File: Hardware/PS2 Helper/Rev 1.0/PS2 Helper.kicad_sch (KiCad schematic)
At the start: 6 parts, among them J1 PORT, J2 Keyboard, U1 74HC595, U2 ATtiny85

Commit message: Housekeeping
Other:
- title: 6502 Keyboard Helper -> 6502 PS2 Helper
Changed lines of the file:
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@@
 	(paper "USLetter")
 	(title_block
-		(title "6502 Keyboard Helper")
-		(date "2025-09-23")
+		(title "6502 PS2 Helper")
+		(date "2025-09-24")
 		(rev "1.0")
 		(company "A.C. Wright Design")

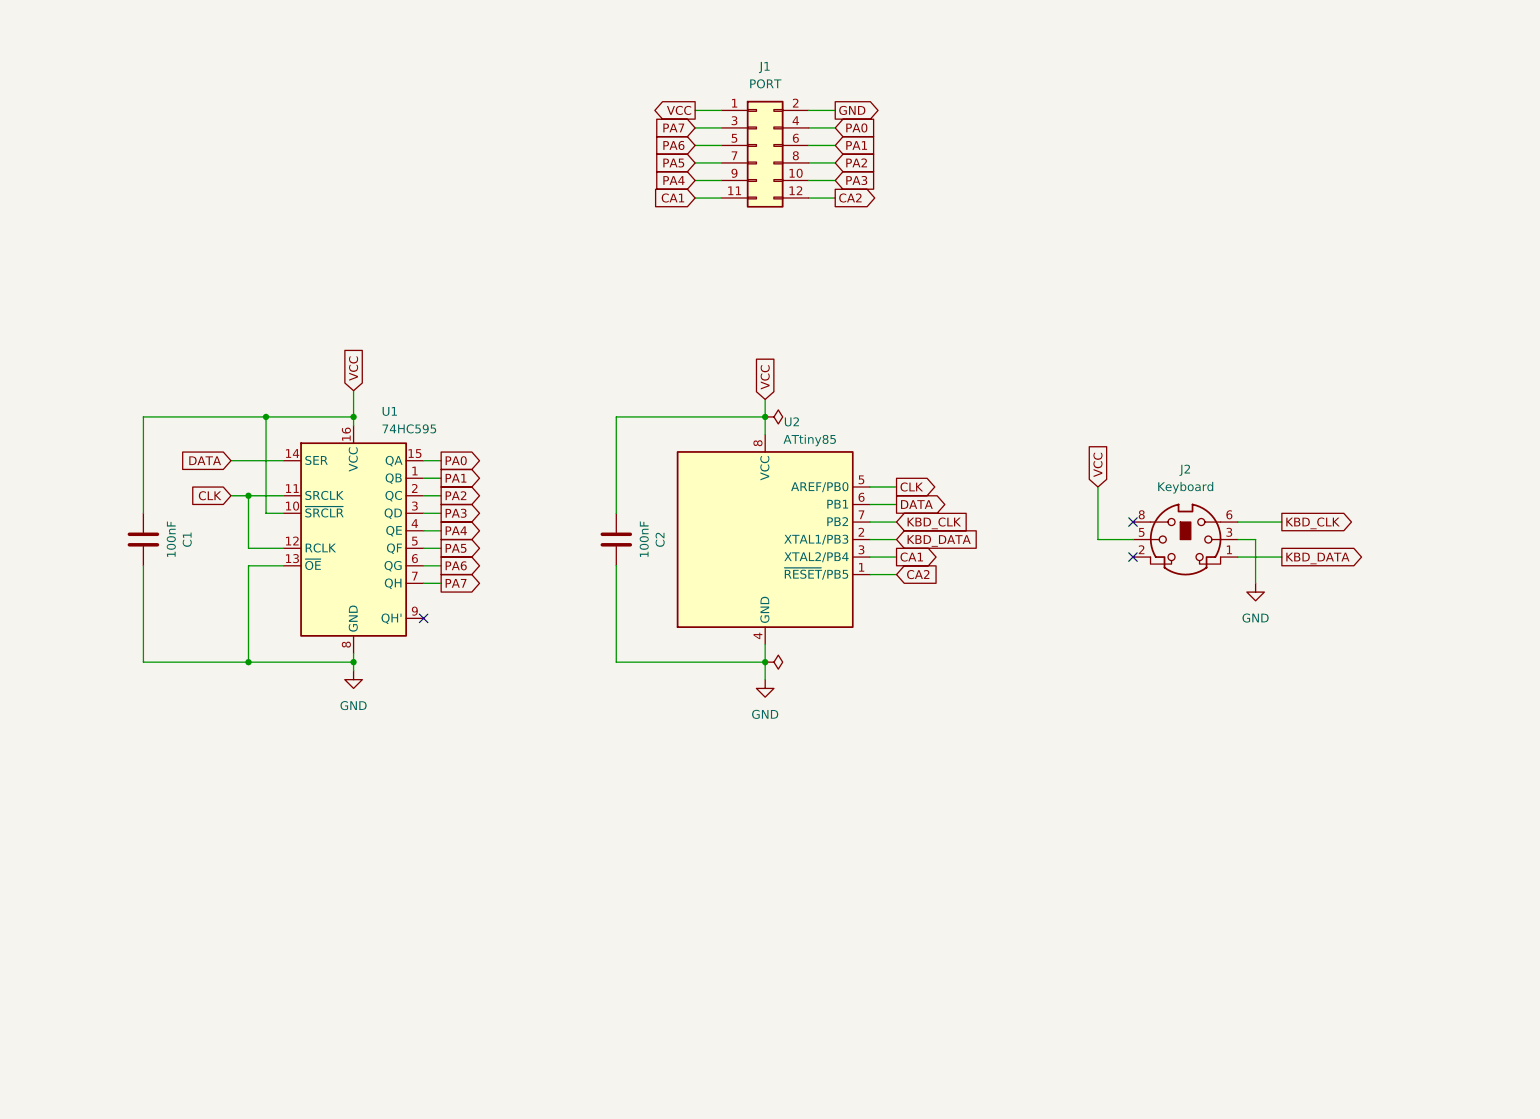
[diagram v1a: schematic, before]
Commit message: Start work on PS2 Helper
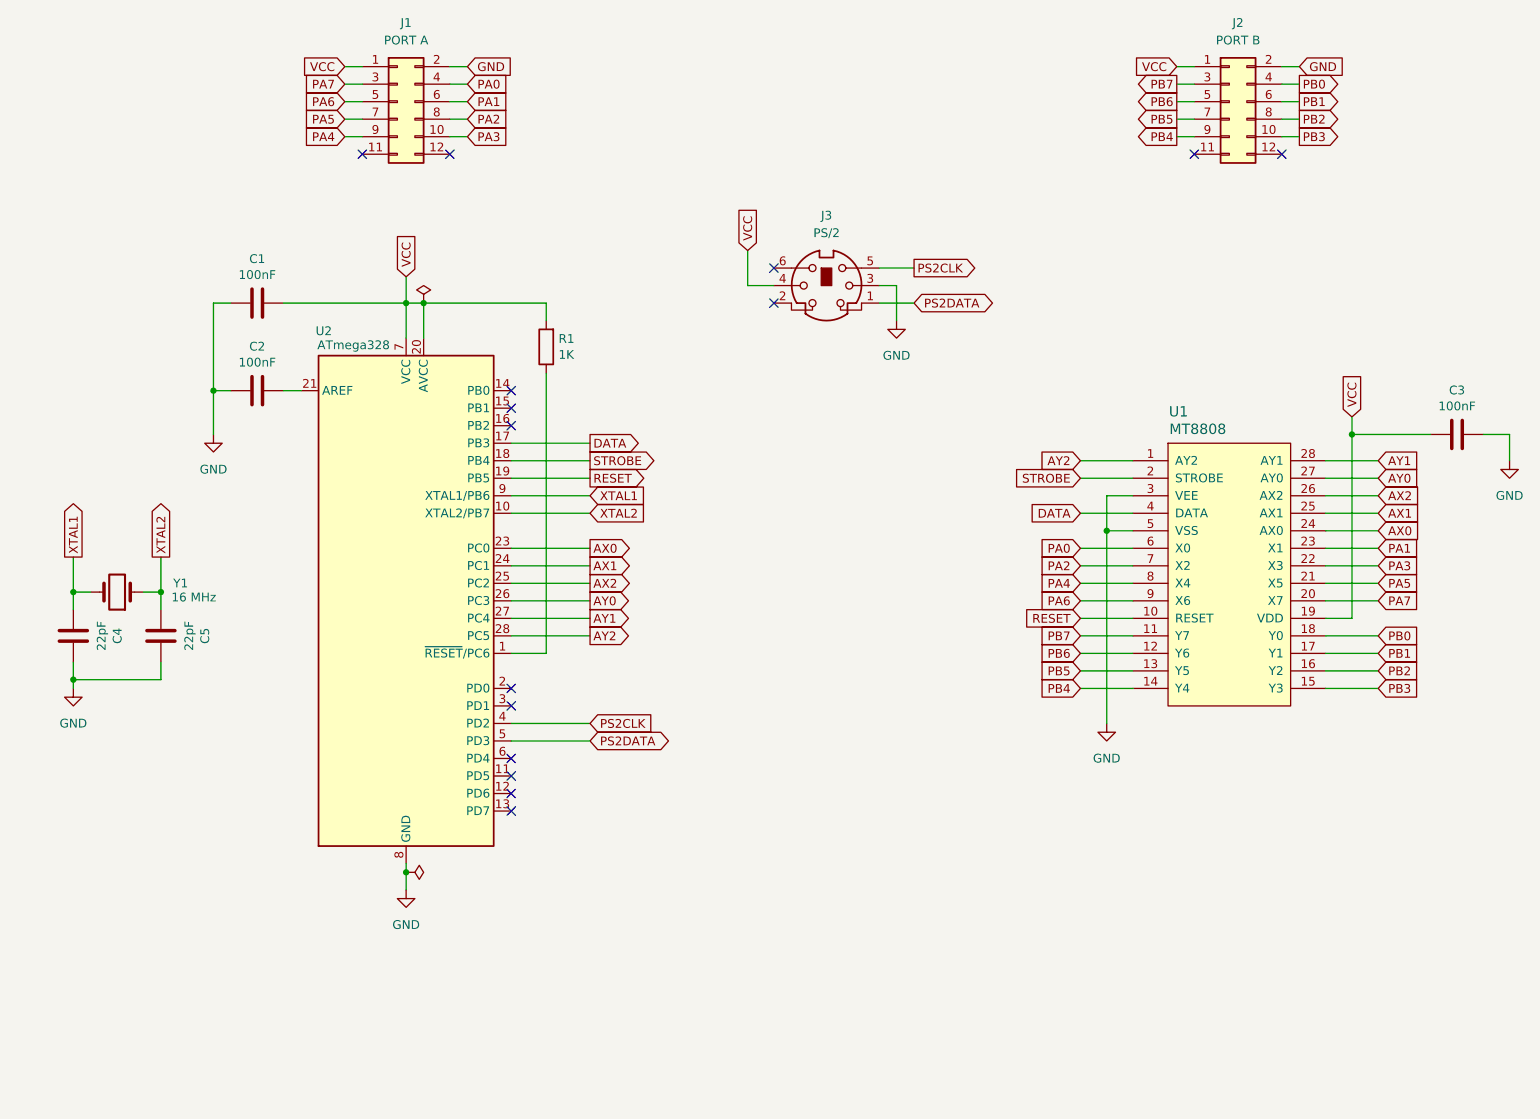
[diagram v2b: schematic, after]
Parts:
- removed J2: Keyboard, 6502 Parts:KMDGX-6S-BS, symbol 6502 Parts:KMDGX-6S-BS
- removed U1: 74HC595, Package_DIP:DIP-16_W7.62mm_Socket_LongPads, symbol 74xx:74HC595
- removed U2: ATtiny85, Package_DIP:DIP-8_W7.62mm_Socket_LongPads, symbol MCU_Microchip_ATtiny:ATtiny85-20P
- added C3: 100nF, Capacitor_THT:C_Disc_D5.0mm_W2.5mm_P2.50mm, symbol Device:C
- added C4, C5: 22pF, Capacitor_THT:C_Disc_D5.0mm_W2.5mm_P2.50mm, symbol Device:C
- added J2: PORT B, 6502 Parts:6502 GPIO Connector, symbol Connector_Generic:Conn_02x06_Odd_Even
- added J3: PS/2, 6502 Parts:KMDGX-6S-BS, symbol 6502 Parts:KMDGX-6S-BS
- added R1: 1K, Resistor_THT:R_Axial_DIN0204_L3.6mm_D1.6mm_P5.08mm_Horizontal, symbol Device:R
- added U1: MT8808, Package_DIP:DIP-28_W15.24mm_Socket_LongPads, symbol 6502 Parts:MT8808
- added U2: ATmega328, Package_DIP:DIP-28_W7.62mm_Socket_LongPads, symbol MCU_Microchip_ATmega:ATmega328-P
- added Y1: 16 MHz, Crystal:Crystal_HC49-U_Vertical, symbol Device:Crystal
- C1, C2: footprint Capacitor_THT:C_Disc_D5.0mm_W2.5mm_P5.00mm -> Capacitor_THT:C_Disc_D5.0mm_W2.5mm_P2.50mm; LCSC C49678 -> C107114; now left out of the parts list
- J1: value PORT -> PORT A
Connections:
- net DATA: now also U1.4 (DATA), U2.17 (PB3)
- net GND: now also C1.1, C2.1, C3.2, C4.2, C5.2, J2.2 (Pin_2), J3.3, U1.3 (VEE), U1.5 (VSS), U2.22 (GND), U2.8 (GND); no longer C1.2, C2.2
- net PA0: now also U1.6 (X0)
- net PA1: now also U1.23 (X1)
- net PA2: now also U1.7 (X2)
- net PA3: now also U1.22 (X3)
- net PA4: now also U1.8 (X4)
- net PA5: now also U1.21 (X5)
- net PA6: now also U1.9 (X6)
- net PA7: now also U1.20 (X7)
- net VCC: now also C1.2, C3.1, J2.1 (Pin_1), J3.4, R1.2, U1.19 (VDD), U2.20 (AVCC), U2.7 (VCC); no longer C1.1, C2.1
- net CA1: no longer names the net of J1.11 (Pin_11)
- net CA2: no longer names the net of J1.12 (Pin_12)
- new net: R1.1, U2.1 (~{RESET}/PC6)
- new net: C2.2, U2.21 (AREF)
- new net AX0: U1.24 (AX0), U2.23 (PC0)
- new net AX1: U1.25 (AX1), U2.24 (PC1)
- new net AX2: U1.26 (AX2), U2.25 (PC2)
- new net AY0: U1.27 (AY0), U2.26 (PC3)
- new net AY1: U1.28 (AY1), U2.27 (PC4)
- new net AY2: U1.1 (AY2), U2.28 (PC5)
- new net PB0: J2.4 (Pin_4), U1.18 (Y0)
- new net PB1: J2.6 (Pin_6), U1.17 (Y1)
- new net PB2: J2.8 (Pin_8), U1.16 (Y2)
- new net PB3: J2.10 (Pin_10), U1.15 (Y3)
- new net PB4: J2.9 (Pin_9), U1.14 (Y4)
- new net PB5: J2.7 (Pin_7), U1.13 (Y5)
- new net PB6: J2.5 (Pin_5), U1.12 (Y6)
- new net PB7: J2.3 (Pin_3), U1.11 (Y7)
- new net PS2CLK: J3.5, U2.4 (PD2)
- new net PS2DATA: J3.1, U2.5 (PD3)
- new net RESET: U1.10 (RESET), U2.19 (PB5)
- new net STROBE: U1.2 (STROBE), U2.18 (PB4)
- new net XTAL1: C4.1, U2.9 (XTAL1/PB6), Y1.2
- new net XTAL2: C5.1, U2.10 (XTAL2/PB7), Y1.1
- no-connect marks 3 -> 15
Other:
- moved on the sheet: J1

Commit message: More parts cleanup
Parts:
- Y1: Digikey (none) -> 3155-16M20P2/49US-ND; Mouser 774-MP107-E -> (none)
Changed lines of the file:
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@@
 			)
 		)
-		(property "Mouser" "774-MP107-E"
+		(property "Digikey" "3155-16M20P2/49US-ND"
 			(at 41.91 121.92 0)
 			(effects

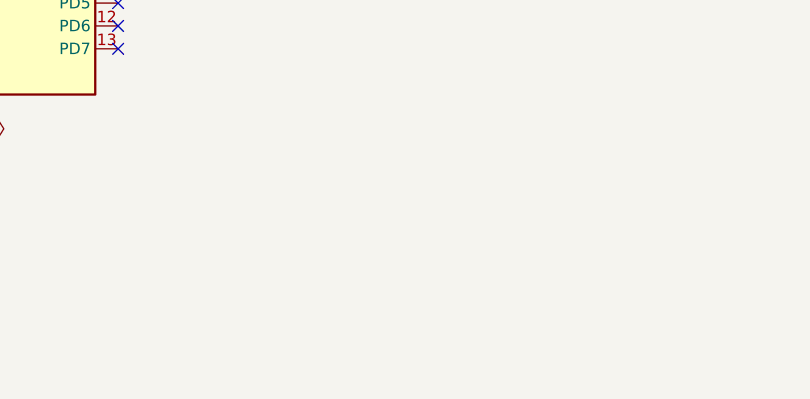
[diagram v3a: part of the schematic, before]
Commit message: Add joystick port to PS2 Helper
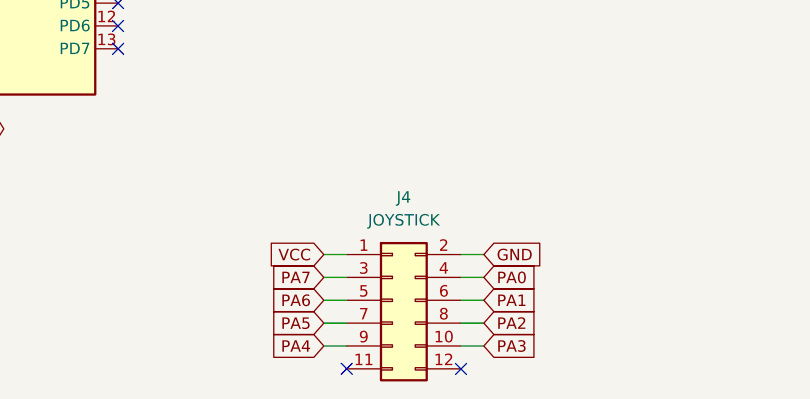
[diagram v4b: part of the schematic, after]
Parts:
- added J4: JOYSTICK, 6502 Parts:6502 GPIO Connector, symbol Connector_Generic:Conn_02x06_Odd_Even
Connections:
- net GND: now also J4.2 (Pin_2)
- net PA0: now also J4.4 (Pin_4)
- net PA1: now also J4.6 (Pin_6)
- net PA2: now also J4.8 (Pin_8)
- net PA3: now also J4.10 (Pin_10)
- net PA4: now also J4.9 (Pin_9)
- net PA5: now also J4.7 (Pin_7)
- net PA6: now also J4.5 (Pin_5)
- net PA7: now also J4.3 (Pin_3)
- net VCC: now also J4.1 (Pin_1)
- no-connect marks 15 -> 17

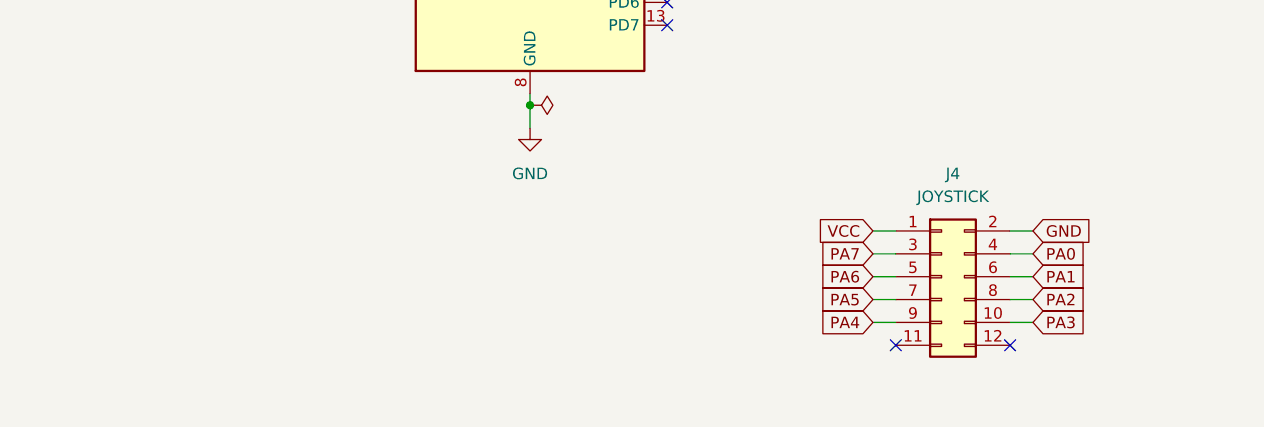
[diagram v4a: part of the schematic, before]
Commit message: Add pullups to PS2 Helper
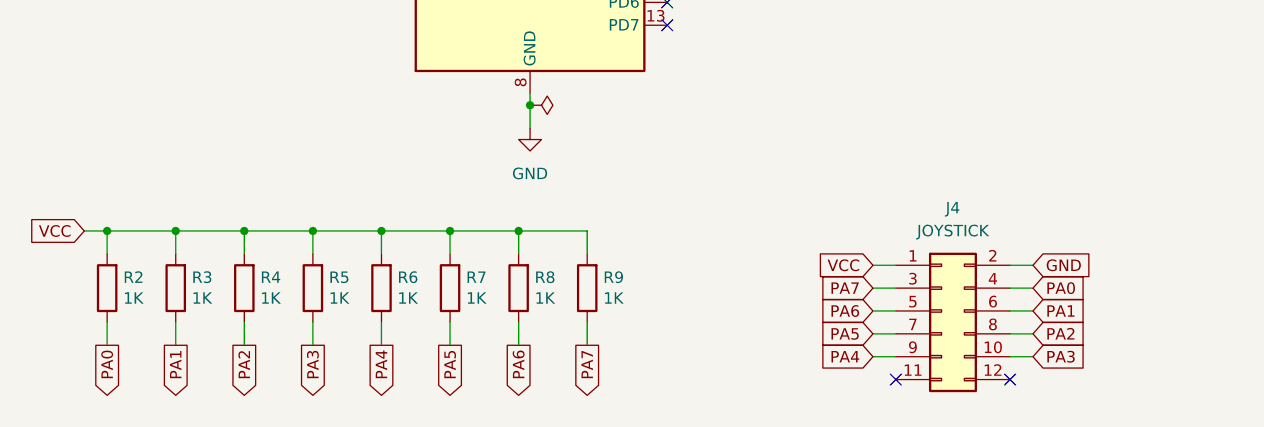
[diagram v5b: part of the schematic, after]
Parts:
- added R2, R3, R4, R5, R6, R7, R8, R9: 1K, Resistor_THT:R_Axial_DIN0204_L3.6mm_D1.6mm_P5.08mm_Horizontal, symbol Device:R
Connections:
- net PA0: now also R2.1
- net PA1: now also R3.1
- net PA2: now also R4.1
- net PA3: now also R5.1
- net PA4: now also R6.1
- net PA5: now also R7.1
- net PA6: now also R8.1
- net PA7: now also R9.1
- net VCC: now also R2.2, R3.2, R4.2, R5.2, R6.2, R7.2, R8.2, R9.2
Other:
- moved on the sheet: J4
